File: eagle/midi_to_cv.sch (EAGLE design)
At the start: 71 parts, among them IC1 TL084P, IC4 TL072P, U1 ATMEGA328P_PDIP, U4 4584N

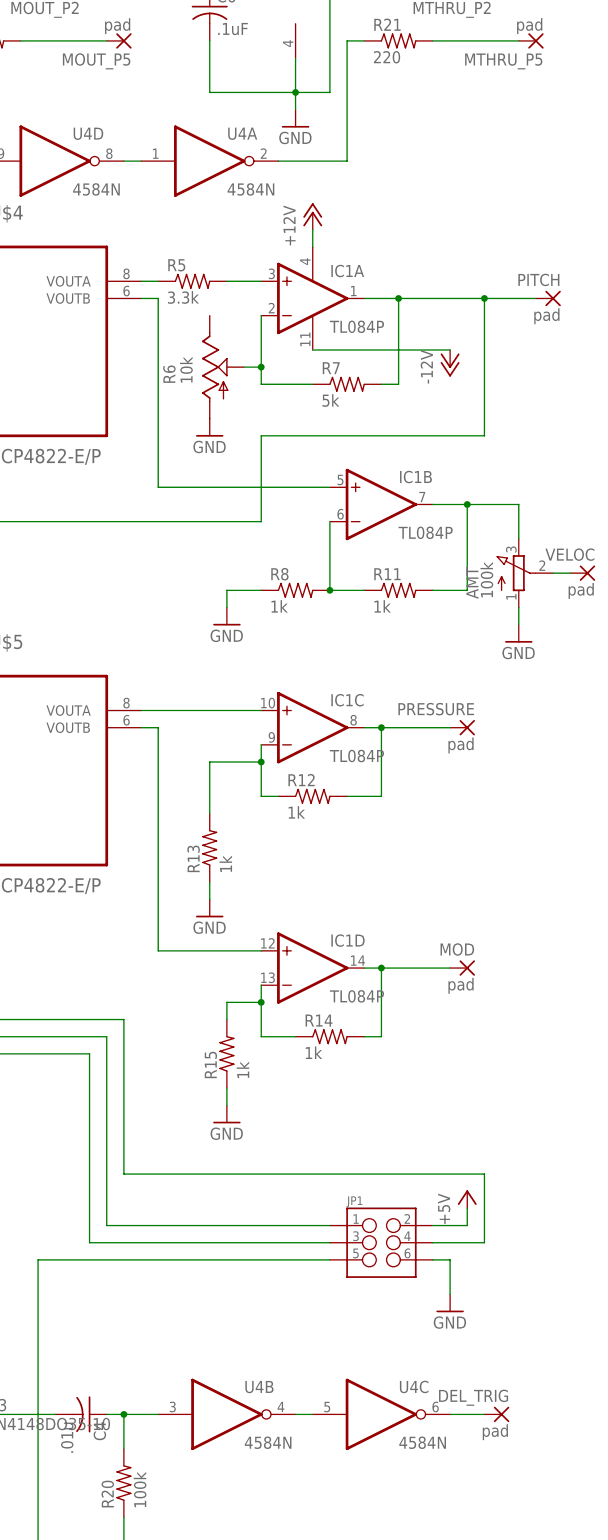
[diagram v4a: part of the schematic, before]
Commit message: swapped some gates and rearranged to layout
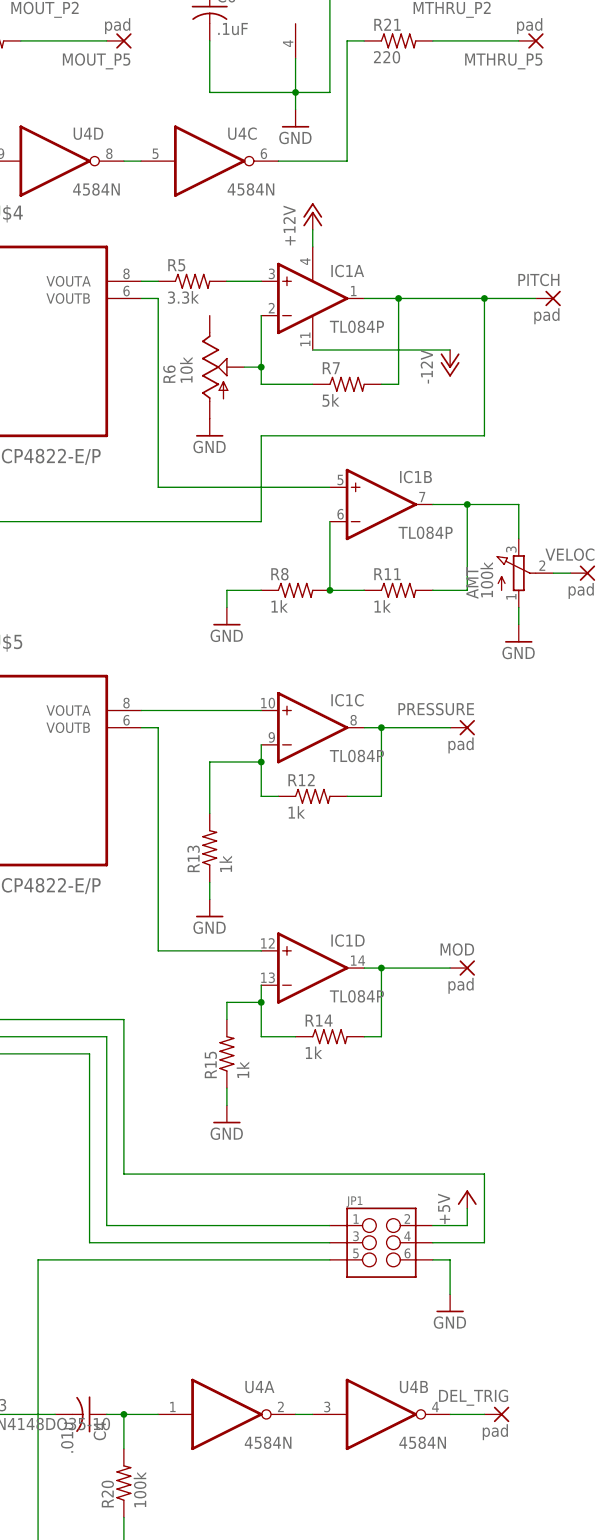
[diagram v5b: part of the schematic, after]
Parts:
- C3, C5, C6: device rcl:C-US025-040X050 -> rcl:C-US050-024X044
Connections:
- net N$39: now also U4C.I; no longer U4A.I
- net N$40: now also U4A.O, U4B.I; no longer U4B.O, U4C.I
- net N$41: now also U4A.I; no longer U4B.I
- net N$49: now also U4B.O; no longer U4C.O
- net N$50: now also U4C.O; no longer U4A.O
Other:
- moved on the sheet: U4A, U4B, U4C
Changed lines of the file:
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@@
 <grid distance="0.1" unitdist="inch" unit="inch" style="lines" multiple="1" display="no" altdistance="0.01" altunitdist="inch" altunit="inch"/>
 <layers>
-<layer number="1" name="Top" color="4" fill="1" visible="yes" active="no"/>
-<layer number="16" name="Bottom" color="1" fill="1" visible="yes" active="no"/>
-<layer number="17" name="Pads" color="2" fill="1" visible="yes" active="no"/>
-<layer number="18" name="Vias" color="2" fill="1" visible="yes" active="no"/>
-<layer number="19" name="Unrouted" color="6" fill="1" visible="yes" active="no"/>
-<layer number="20" name="Dimension" color="15" fill="1" visible="yes" active="no"/>
-<layer number="21" name="tPlace" color="7" fill="1" visible="yes" active="no"/>
-<layer number="22" name="bPlace" color="7" fill="1" visible="yes" active="no"/>
-<layer number="23" name="tOrigins" color="15" fill="1" visible="yes" active="no"/>
-<layer number="24" name="bOrigins" color="15" fill="1" visible="yes" active="no"/>
-<layer number="25" name="tNames" color="7" fill="1" visible="yes" active="no"/>
-<layer number="26" name="bNames" color="7" fill="1" visible="yes" active="no"/>
-<layer number="27" name="tValues" color="7" fill="1" visible="yes" active="no"/>
-<layer number="28" name="bValues" color="7" fill="1" visible="yes" active="no"/>
+<layer number="1" name="Top" color="4" fill="1" visible="no" active="no"/>
+<layer number="16" name="Bottom" color="1" fill="1" visible="no" active="no"/>
+<layer number="17" name="Pads" color="2" fill="1" visible="no" active="no"/>
+<layer number="18" name="Vias" color="2" fill="1" visible="no" active="no"/>
+<layer number="19" name="Unrouted" color="6" fill="1" visible="no" active="no"/>
+<layer number="20" name="Dimension" color="15" fill="1" visible="no" active="no"/>
+<layer number="21" name="tPlace" color="7" fill="1" visible="no" active="no"/>
+<layer number="22" name="bPlace" color="7" fill="1" visible="no" active="no"/>
+<layer number="23" name="tOrigins" color="15" fill="1" visible="no" active="no"/>
+<layer number="24" name="bOrigins" color="15" fill="1" visible="no" active="no"/>
+<layer number="25" name="tNames" color="7" fill="1" visible="no" active="no"/>
+<layer number="26" name="bNames" color="7" fill="1" visible="no" active="no"/>
+<layer number="27" name="tValues" color="7" fill="1" visible="no" active="no"/>
+<layer number="28" name="bValues" color="7" fill="1" visible="no" active="no"/>
 <layer number="29" name="tStop" color="7" fill="3" visible="no" active="no"/>
 <layer number="30" name="bStop" color="7" fill="6" visible="no" active="no"/>
@@
 <layer number="35" name="tGlue" color="7" fill="4" visible="no" active="no"/>
 <layer number="36" name="bGlue" color="7" fill="5" visible="no" active="no"/>
-<layer number="37" name="tTest" color="7" fill="1" visible="yes" active="no"/>
-<layer number="38" name="bTest" color="7" fill="1" visible="yes" active="no"/>
+<layer number="37" name="tTest" color="7" fill="1" visible="no" active="no"/>
+<layer number="38" name="bTest" color="7" fill="1" visible="no" active="no"/>
 <layer number="39" name="tKeepout" color="4" fill="11" visible="no" active="no"/>
 <layer number="40" name="bKeepout" color="1" fill="11" visible="no" active="no"/>
@@
 <layer number="44" name="Drills" color="7" fill="1" visible="no" active="no"/>
 <layer number="45" name="Holes" color="7" fill="1" visible="no" active="no"/>
-<layer number="46" name="Milling" color="3" fill="1" visible="yes" active="no"/>
-<layer number="47" name="Measures" color="7" fill="1" visible="yes" active="no"/>
-<layer number="48" name="Document" color="7" fill="1" visible="yes" active="no"/>
-<layer number="49" name="Reference" color="7" fill="1" visible="yes" active="no"/>
-<layer number="50" name="dxf" color="7" fill="1" visible="yes" active="no"/>
-<layer number="51" name="tDocu" color="7" fill="1" visible="yes" active="no"/>
-<layer number="52" name="bDocu" color="7" fill="1" visible="yes" active="no"/>
-<layer number="53" name="tGND_GNDA" color="7" fill="9" visible="yes" active="no"/>
-<layer number="54" name="bGND_GNDA" color="1" fill="9" visible="yes" active="no"/>
-<layer number="56" name="wert" color="7" fill="1" visible="yes" active="no"/>
-<layer number="57" name="tCAD" color="7" fill="1" visible="yes" active="no"/>
+<layer number="46" name="Milling" color="3" fill="1" visible="no" active="no"/>
+<layer number="47" name="Measures" color="7" fill="1" visible="no" active="no"/>
+<layer number="48" name="Document" color="7" fill="1" visible="no" active="no"/>
+<layer number="49" name="Reference" color="7" fill="1" visible="no" active="no"/>
+<layer number="50" name="dxf" color="7" fill="1" visible="no" active="no"/>
+<layer number="51" name="tDocu" color="7" fill="1" visible="no" active="no"/>
+<layer number="52" name="bDocu" color="7" fill="1" visible="no" active="no"/>
+<layer number="53" name="tGND_GNDA" color="7" fill="9" visible="no" active="no"/>
+<layer number="54" name="bGND_GNDA" color="1" fill="9" visible="no" active="no"/>
+<layer number="56" name="wert" color="7" fill="1" visible="no" active="no"/>
+<layer number="57" name="tCAD" color="7" fill="1" visible="no" active="no"/>
 <layer number="90" name="Modules" color="5" fill="1" visible="yes" active="yes"/>
 <layer number="91" name="Nets" color="2" fill="1" visible="yes" active="yes"/>
@@
 <part name="R1" library="rcl" deviceset="R-US_" device="0207/10" value="10k"/>
 <part name="OK1" library="optocoupler" deviceset="6N138" device=""/>
-<part name="C3" library="rcl" deviceset="C-US" device="025-040X050" value=".1uF"/>
+<part name="C3" library="rcl" deviceset="C-US" device="050-024X044" value=".1uF"/>
 <part name="IC1" library="linear" deviceset="TL084" device="P"/>
 <part name="D1" library="diode" deviceset="1N4148" device="DO35-10"/>
@@
 <part name="AMT" library="pot" deviceset="3RP/1610N" device="" value="100k"/>
 <part name="GND19" library="supply1" deviceset="GND" device=""/>
-<part name="C6" library="rcl" deviceset="C-US" device="025-040X050" value=".1uF"/>
+<part name="C6" library="rcl" deviceset="C-US" device="050-024X044" value=".1uF"/>
 <part name="P+13" library="supply1" deviceset="+5V" device=""/>
 <part name="GND20" library="supply1" deviceset="GND" device=""/>
@@
 <part name="MTHRU_P2" library="wirepad" deviceset="2,54/0,9" device="" value="pad"/>
 <part name="R22" library="rcl" deviceset="R-US_" device="0207/10" value="220"/>
-<part name="C5" library="rcl" deviceset="C-US" device="025-040X050" value=".1uF"/>
+<part name="C5" library="rcl" deviceset="C-US" device="050-024X044" value=".1uF"/>
 <part name="P+14" library="supply1" deviceset="+5V" device=""/>
 <part name="GND17" library="supply1" deviceset="GND" device=""/>
@@
 <instance part="P+11" gate="1" x="45.72" y="137.16"/>
 <instance part="GND16" gate="1" x="45.72" y="111.76"/>
-<instance part="U4" gate="A" x="134.62" y="147.32"/>
-<instance part="U4" gate="B" x="137.16" y="-38.1"/>
-<instance part="U4" gate="C" x="160.02" y="-38.1"/>
+<instance part="U4" gate="A" x="137.16" y="-38.1"/>
+<instance part="U4" gate="B" x="160.02" y="-38.1"/>
+<instance part="U4" gate="C" x="134.62" y="147.32"/>
 <instance part="U4" gate="D" x="111.76" y="147.32"/>
 <instance part="U4" gate="E" x="17.78" y="147.32" smashed="yes">
@@
 </segment>
 </net>
-<net name="N$39" class="0">
-<segment>
-<pinref part="U4" gate="D" pin="O"/>
-<pinref part="U4" gate="A" pin="I"/>
-<wire x1="121.92" y1="147.32" x2="124.46" y2="147.32" width="0.1524" layer="91"/>
-</segment>
-</net>
-<net name="N$40" class="0">
-<segment>
-<pinref part="U4" gate="B" pin="O"/>
-<pinref part="U4" gate="C" pin="I"/>
-<wire x1="149.86" y1="-38.1" x2="147.32" y2="-38.1" width="0.1524" layer="91"/>
-</segment>
-</net>
 <net name="N$41" class="0">
 <segment>
-<pinref part="U4" gate="B" pin="I"/>
 <pinref part="C4" gate="G$1" pin="1"/>
 <wire x1="119.38" y1="-38.1" x2="121.92" y2="-38.1" width="0.1524" layer="91"/>
 <pinref part="R20" gate="G$1" pin="2"/>
-<wire x1="121.92" y1="-38.1" x2="127" y2="-38.1" width="0.1524" layer="91"/>
 <wire x1="121.92" y1="-43.18" x2="121.92" y2="-38.1" width="0.1524" layer="91"/>
+<pinref part="U4" gate="A" pin="I"/>
+<wire x1="127" y1="-38.1" x2="121.92" y2="-38.1" width="0.1524" layer="91"/>
 <junction x="121.92" y="-38.1"/>
 </segment>
@@
 </segment>
 </net>
-<net name="N$49" class="0">
-<segment>
-<pinref part="U4" gate="C" pin="O"/>
-<pinref part="DEL_TRIG" gate="1" pin="P"/>
-<wire x1="175.26" y1="-38.1" x2="170.18" y2="-38.1" width="0.1524" layer="91"/>
-</segment>
-</net>
 <net name="N$50" class="0">
 <segment>
-<pinref part="U4" gate="A" pin="O"/>
 <pinref part="R21" gate="G$1" pin="1"/>
 <wire x1="157.48" y1="165.1" x2="154.94" y2="165.1" width="0.1524" layer="91"/>
+<wire x1="154.94" y1="147.32" x2="154.94" y2="165.1" width="0.1524" layer="91"/>
+<pinref part="U4" gate="C" pin="O"/>
 <wire x1="144.78" y1="147.32" x2="154.94" y2="147.32" width="0.1524" layer="91"/>
-<wire x1="154.94" y1="147.32" x2="154.94" y2="165.1" width="0.1524" layer="91"/>
 </segment>
 </net>
@@
 </segment>
 </net>
+<net name="N$39" class="0">
+<segment>
+<pinref part="U4" gate="D" pin="O"/>
+<pinref part="U4" gate="C" pin="I"/>
+<wire x1="124.46" y1="147.32" x2="121.92" y2="147.32" width="0.1524" layer="91"/>
+</segment>
+</net>
+<net name="N$40" class="0">
+<segment>
+<pinref part="U4" gate="A" pin="O"/>
+<pinref part="U4" gate="B" pin="I"/>
+<wire x1="149.86" y1="-38.1" x2="147.32" y2="-38.1" width="0.1524" layer="91"/>
+</segment>
+</net>
+<net name="N$49" class="0">
+<segment>
+<pinref part="U4" gate="B" pin="O"/>
+<pinref part="DEL_TRIG" gate="1" pin="P"/>
+<wire x1="170.18" y1="-38.1" x2="175.26" y2="-38.1" width="0.1524" layer="91"/>
+</segment>
+</net>

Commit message: ready to cut layout
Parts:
- R18, R27: value 20k -> 47k
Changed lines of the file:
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@@
 <part name="R10" library="rcl" deviceset="R-US_" device="0207/10" value="1k"/>
 <part name="R17" library="rcl" deviceset="R-US_" device="0207/10" value="10k"/>
-<part name="R18" library="rcl" deviceset="R-US_" device="0207/10" value="20k"/>
+<part name="R18" library="rcl" deviceset="R-US_" device="0207/10" value="47k"/>
 <part name="R26" library="rcl" deviceset="R-US_" device="0207/10" value="1k"/>
 <part name="GND14" library="supply1" deviceset="GND" device=""/>
-<part name="R27" library="rcl" deviceset="R-US_" device="0207/10" value="20k"/>
+<part name="R27" library="rcl" deviceset="R-US_" device="0207/10" value="47k"/>
 <part name="R28" library="rcl" deviceset="R-US_" device="0207/10" value="10k"/>
 <part name="R29" library="rcl" deviceset="R-US_" device="0207/10" value="1k"/>
